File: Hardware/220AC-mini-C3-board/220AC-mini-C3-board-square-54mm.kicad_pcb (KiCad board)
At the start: 2 copper layers, 52.7 x 52.7 mm, 18 parts, among them J1 AC MAINS POWER, J2 ON/OFF switch, J3 Conn_01x04, K1 HF163-F, Q1 Q_NPN_CBE, Q2 Q_NPN_CBE, U1 PBO-3C-3

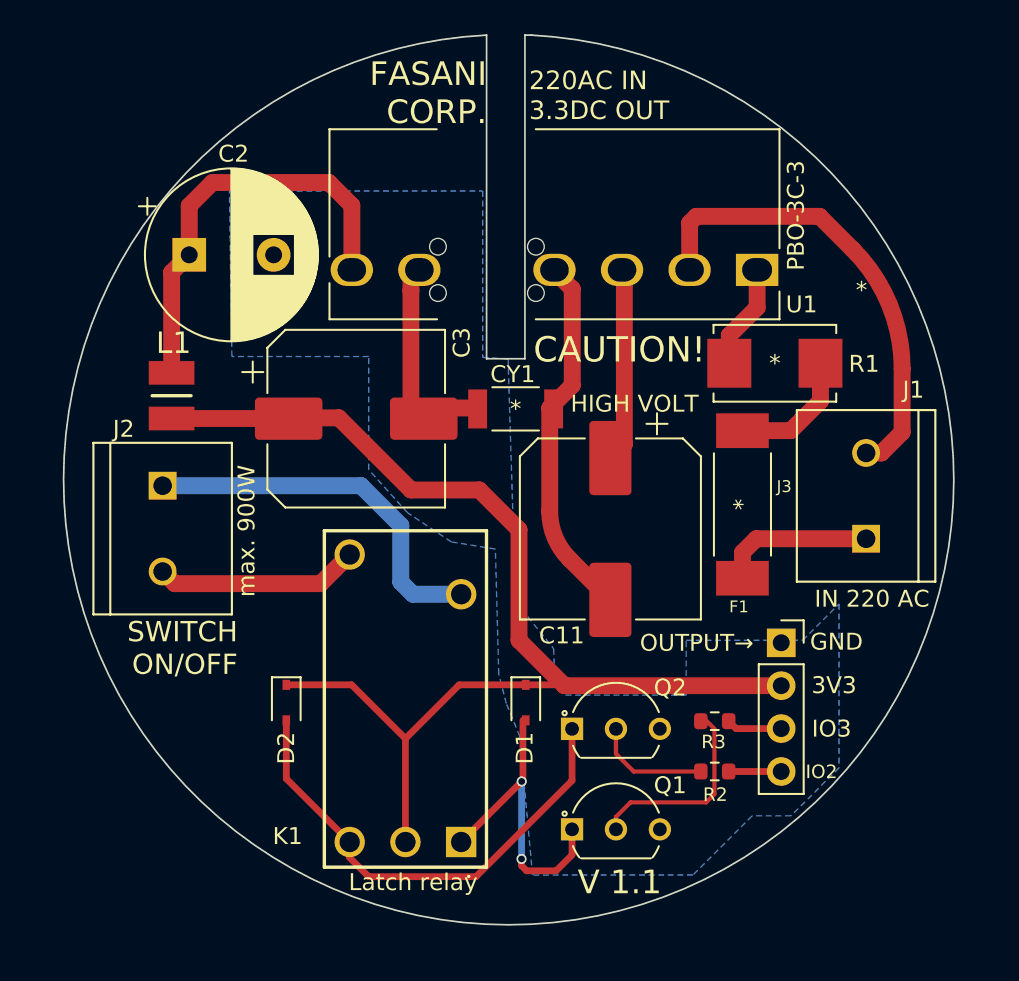
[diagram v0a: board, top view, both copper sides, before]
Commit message: 220AC 3.3DC adapter redesigned 1.1
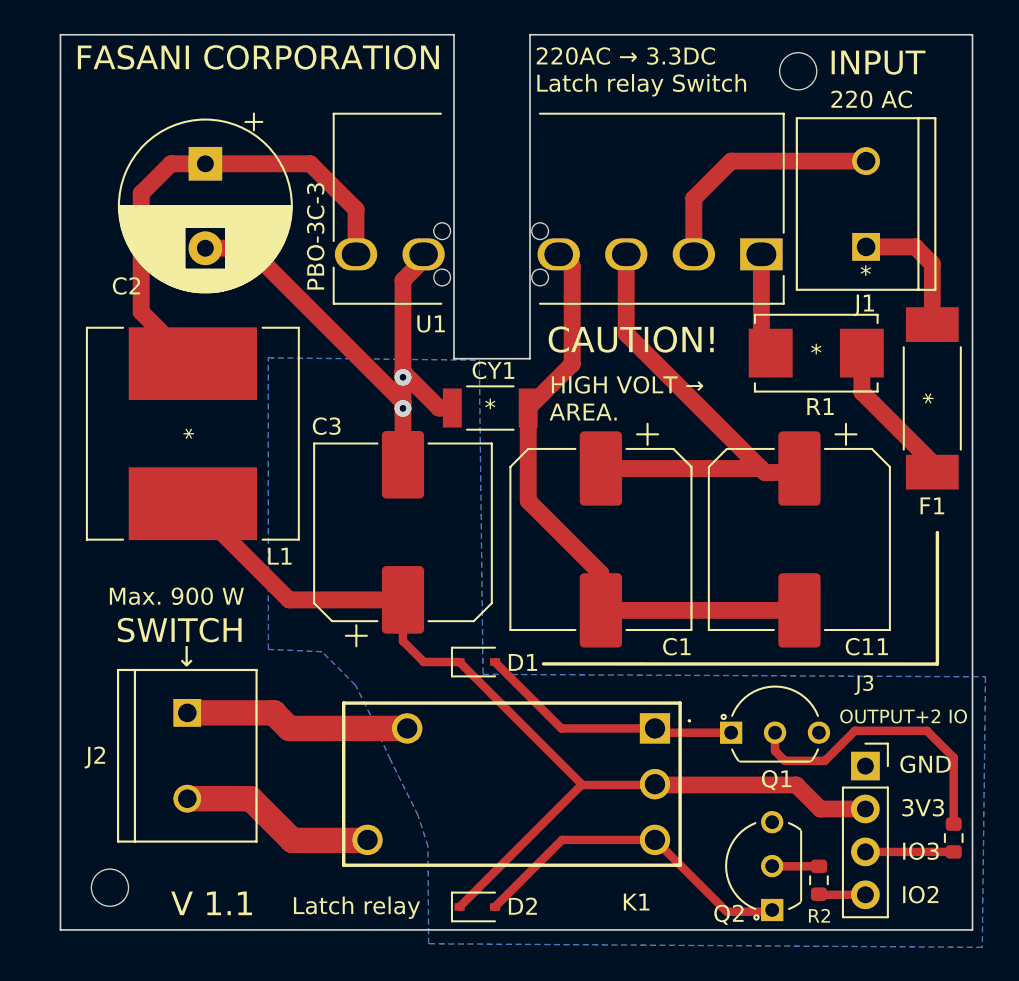
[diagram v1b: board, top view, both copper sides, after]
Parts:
- added C1: 12uF, Capacitor_SMD:CP_Elec_10x14.3, F.Cu at (142.0, 88.9)
- added H2: MountingHole, footprint:MountingHole_2.2mm_M2, F.Cu at (153.7, 61.2)
- added H4: MountingHole, footprint:MountingHole_2.2mm_M2, F.Cu at (112.9, 109.5)
- L1: footprint footprint:IND_BRL3225T4R7M -> footprint:SMDRI127-470MT
- moved J1 17.3 mm to (157.7, 69.0)
- moved D2 16.6 mm to (134.7, 110.6), turned to 0 degrees
- moved Q2 16.0 mm to (152.1, 110.8), turned to 90 degrees
- moved R3 15.8 mm to (162.9, 106.6), turned to -90 degrees
- moved J2 13.5 mm to (117.5, 101.7)
- moved F1 12.9 mm to (161.6, 80.5), turned to -90 degrees
- moved C11 11.2 mm to (153.8, 88.9)
- moved Q1 11.0 mm to (149.7, 100.3)
- moved R2 8.92 mm to (154.9, 109.1), turned to -90 degrees
- moved J3 8.84 mm to (157.7, 102.3)
- moved K1 7.90 mm to (136.5, 103.3), turned to 180 degrees
- moved C3 7.28 mm to (130.3, 88.5), turned to 90 degrees
- moved C2 5.47 mm to (118.6, 66.6), turned to -90 degrees
- moved D1 3.74 mm to (134.7, 96.1), turned to 0 degrees
- moved L1 2.58 mm to (117.8, 82.6)
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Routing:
- net GND: track 12.6 -> 32.2 mm, vias 0 -> 2
- net Net-(C1-Pad1): track 11.3 -> 28.2 mm
- net Net-(C1-Pad2): track 21.5 -> 36.1 mm
- net /AC (N): track 27.6 -> 14.4 mm
- net +3V3: track 71.8 -> 59.0 mm
- net Net-(D2-Pad2): track 28.7 -> 19.2 mm
- net Net-(J2-Pad1): track 22.3 -> 13.4 mm
- net Net-(Q1-Pad2): track 11.8 -> 17.2 mm
- net Net-(Q2-Pad2): track 6.93 -> 2.78 mm
- net Net-(C2-Pad1): track 24.9 -> 28.6 mm
- net Net-(D1-Pad2): track 18.7 -> 15.7 mm, vias 2 -> 0
- net /IO_3: track 3.29 -> 5.23 mm
- net AC: track 9.18 -> 7.93 mm
- net Net-(F1-Pad2): track 7.58 -> 8.78 mm
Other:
- board size 52.7 x 52.7 mm -> 54 x 53 mm
- board text added: "220 AC"
- board text added: "220AC → 3.3DC Latch relay Switch"
- board text added: "FASANI CORPORATION"
- board text added: "HIGH VOLT → AREA."
- board text added: "INPUT"
- board text added: "Max. 900 W"
- board text added: "OUTPUT+2 IO"
- board text added: "SWITCH"
- board text added: "↓"
- board text removed: "220AC IN 3.3DC OUT"
- board text removed: "FASANI CORP."
- board text removed: "HIGH VOLT"
- board text removed: "IN 220 AC"
- board text removed: "OUTPUT→"
- board text removed: "SWITCH ON/OFF"
- board text removed: "max. 900W"
